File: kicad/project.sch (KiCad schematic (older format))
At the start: 21 parts, among them J1 SWD, U1 STM32L031F4Px

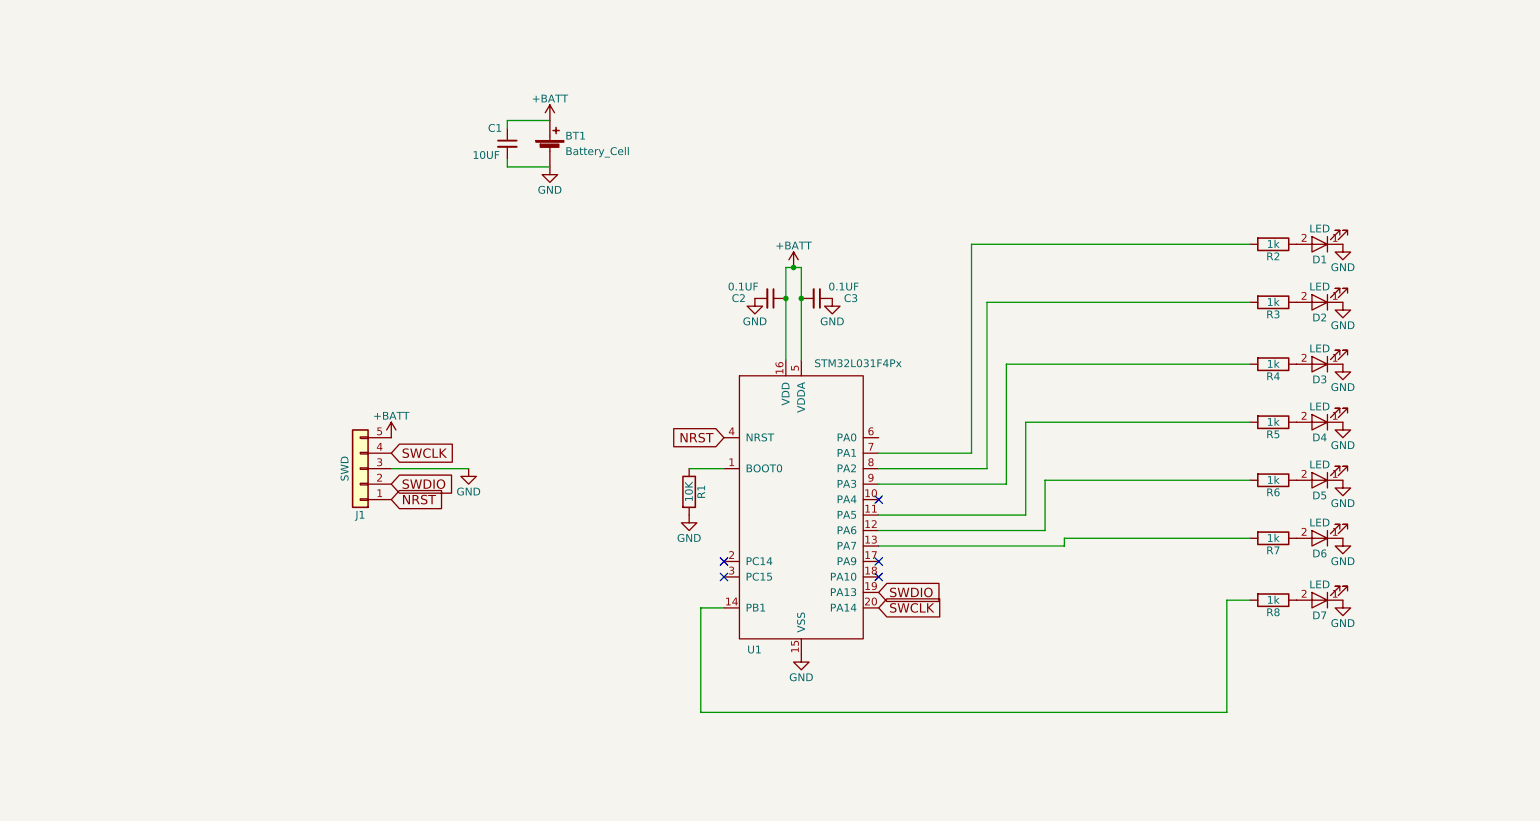
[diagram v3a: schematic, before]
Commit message: Power switch
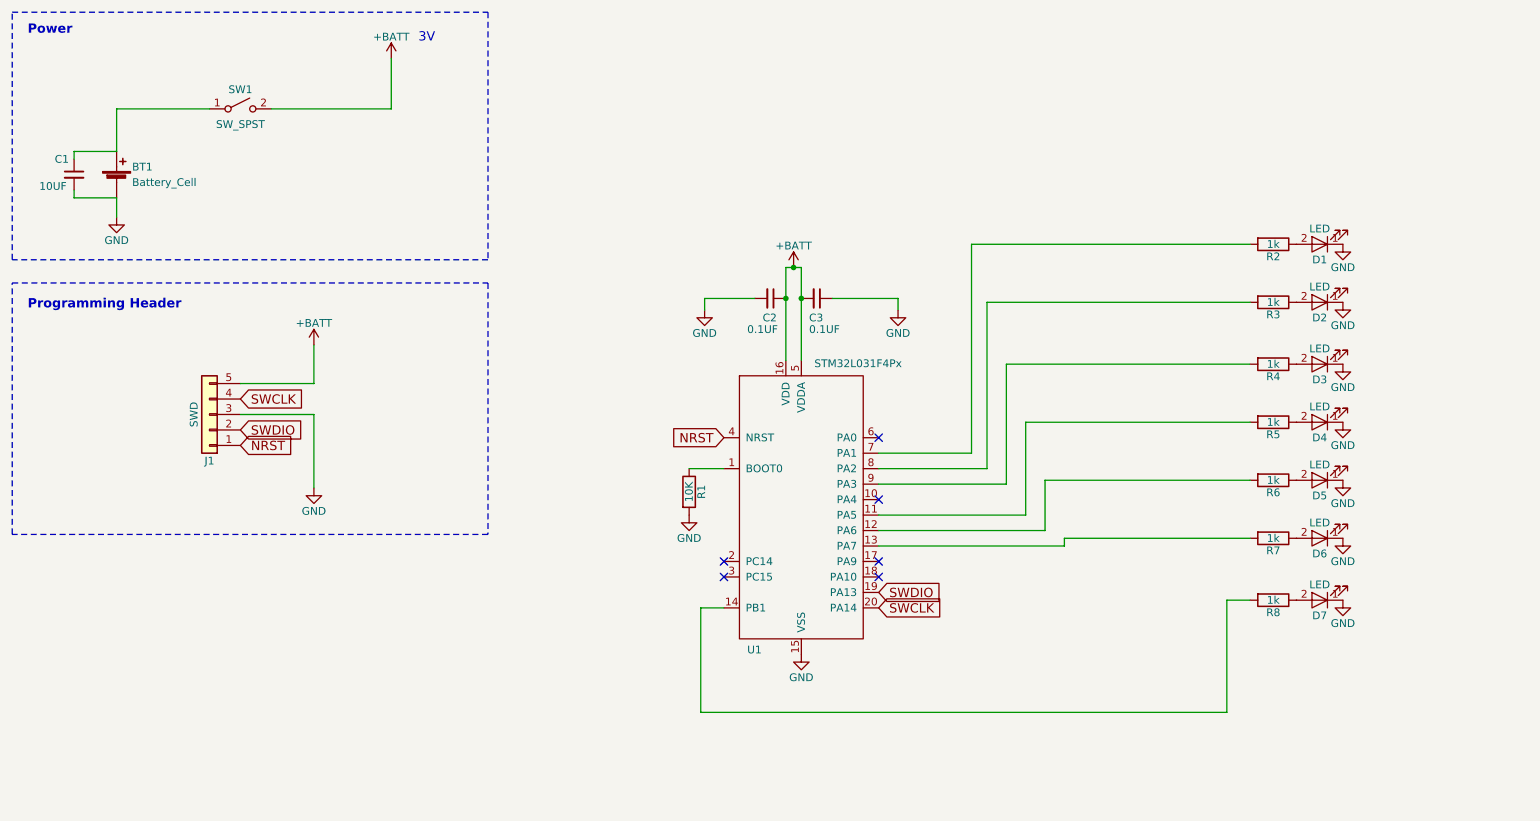
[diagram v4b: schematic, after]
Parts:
- added SW1: SW_SPST, Buttons_Switches_THT:SW_Tactile_Straight_KSA0Axx1LFTR, symbol SW_SPST
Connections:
- net +BATT: now also SW1.2 (B); no longer BT1.1 (+), C1.1
- new net: BT1.1 (+), C1.1, SW1.1 (A)
- no-connect marks 5 -> 6
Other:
- note added: "3V"
- note added: "Power"
- note added: "Programming Header"
- moved on the sheet: BT1, C1, J1

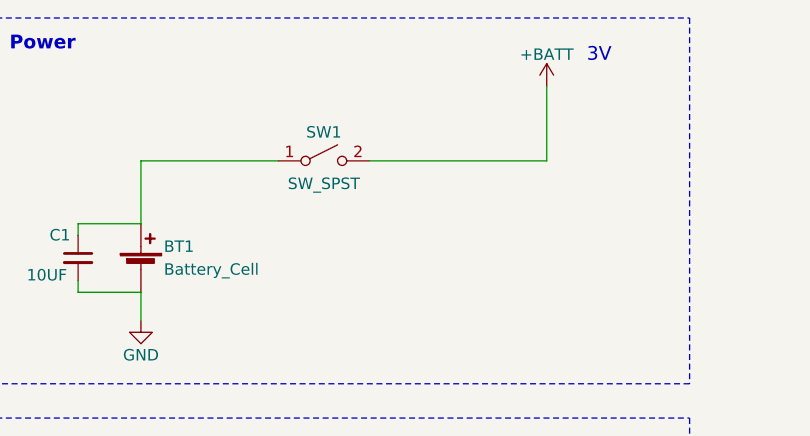
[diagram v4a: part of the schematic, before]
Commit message: 3 pin push switch
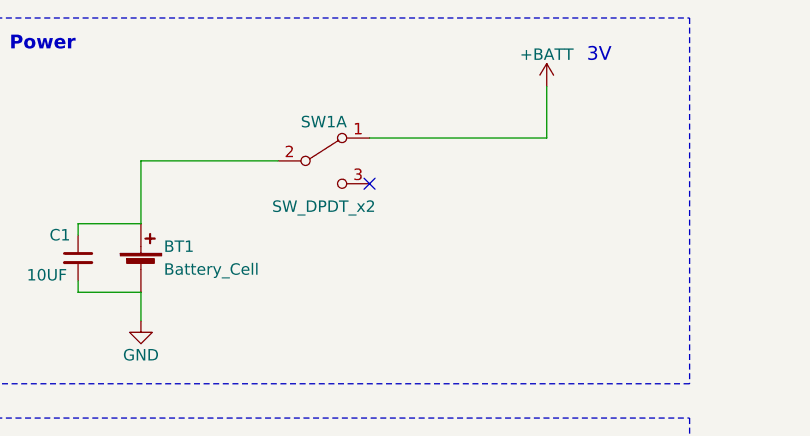
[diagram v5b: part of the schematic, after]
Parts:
- removed SW1: SW_SPST, Buttons_Switches_THT:SW_Tactile_Straight_KSA0Axx1LFTR, symbol SW_SPST
- added SW1: SW_DPDT_x2, Buttons_Switches_THT:SW_Micro_SPST, symbol SW_DPDT_x2
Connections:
- net +BATT: now also SW1.1 (A)
- net at BT1.1 (+), C1.1: now also SW1.2 (B)
- no-connect marks 6 -> 7
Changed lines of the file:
@@
 Wire Wire Line
 	1250 1300 1250 1575
-Wire Wire Line
-	2250 1300 3025 1300
 Text Notes 3200 875  0    60   ~ 0
 3V
@@
 	1250 1300 1850 1300
 Wire Wire Line
-	3025 1300 3025 975
-Wire Wire Line
 	1250 2000 1250 1875
-$Comp
-L SW_SPST SW1
-U 1 1 5AA2904E
-P 2050 1300
-F 0 "SW1" H 2050 1425 50  0000 C CNN
-F 1 "SW_SPST" H 2050 1200 50  0000 C CNN
-F 2 "Buttons_Switches_THT:SW_Tactile_Straight_KSA0Axx1LFTR" H 2050 1300 50  0001 C CNN
-F 3 "" H 2050 1300 50  0001 C CNN
-	1    2050 1300
-	1    0    0    -1
-$EndComp
 Wire Notes Line
 	575  2425 3650 2425
@@
 	6300 2525 6300 2600
 NoConn ~ 6175 3425
+$Comp
+L SW_DPDT_x2 SW1
+U 1 1 5AA401EC
+P 2050 1300
+F 0 "SW1" H 2050 1470 50  0000 C CNN
+F 1 "SW_DPDT_x2" H 2050 1100 50  0000 C CNN
+F 2 "Buttons_Switches_THT:SW_Micro_SPST" H 2050 1300 50  0001 C CNN
+F 3 "" H 2050 1300 50  0001 C CNN
+	1    2050 1300
+	1    0    0    -1
+$EndComp
+Wire Wire Line
+	2250 1200 3025 1200
+Wire Wire Line
+	3025 1200 3025 975
+NoConn ~ 2250 1400
 $EndSCHEMATC

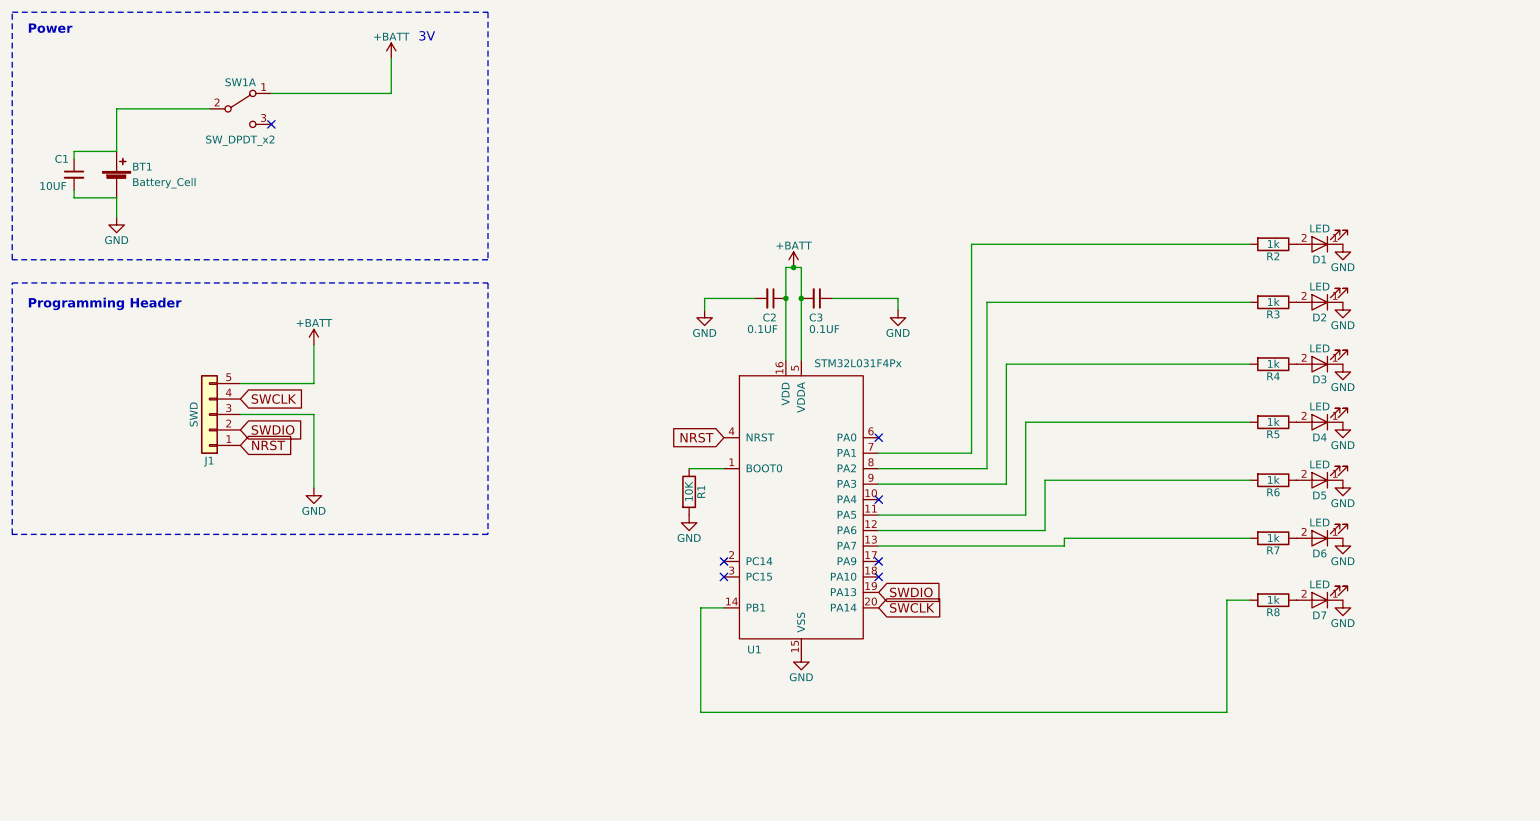
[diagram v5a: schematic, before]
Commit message: Optional LED footprints
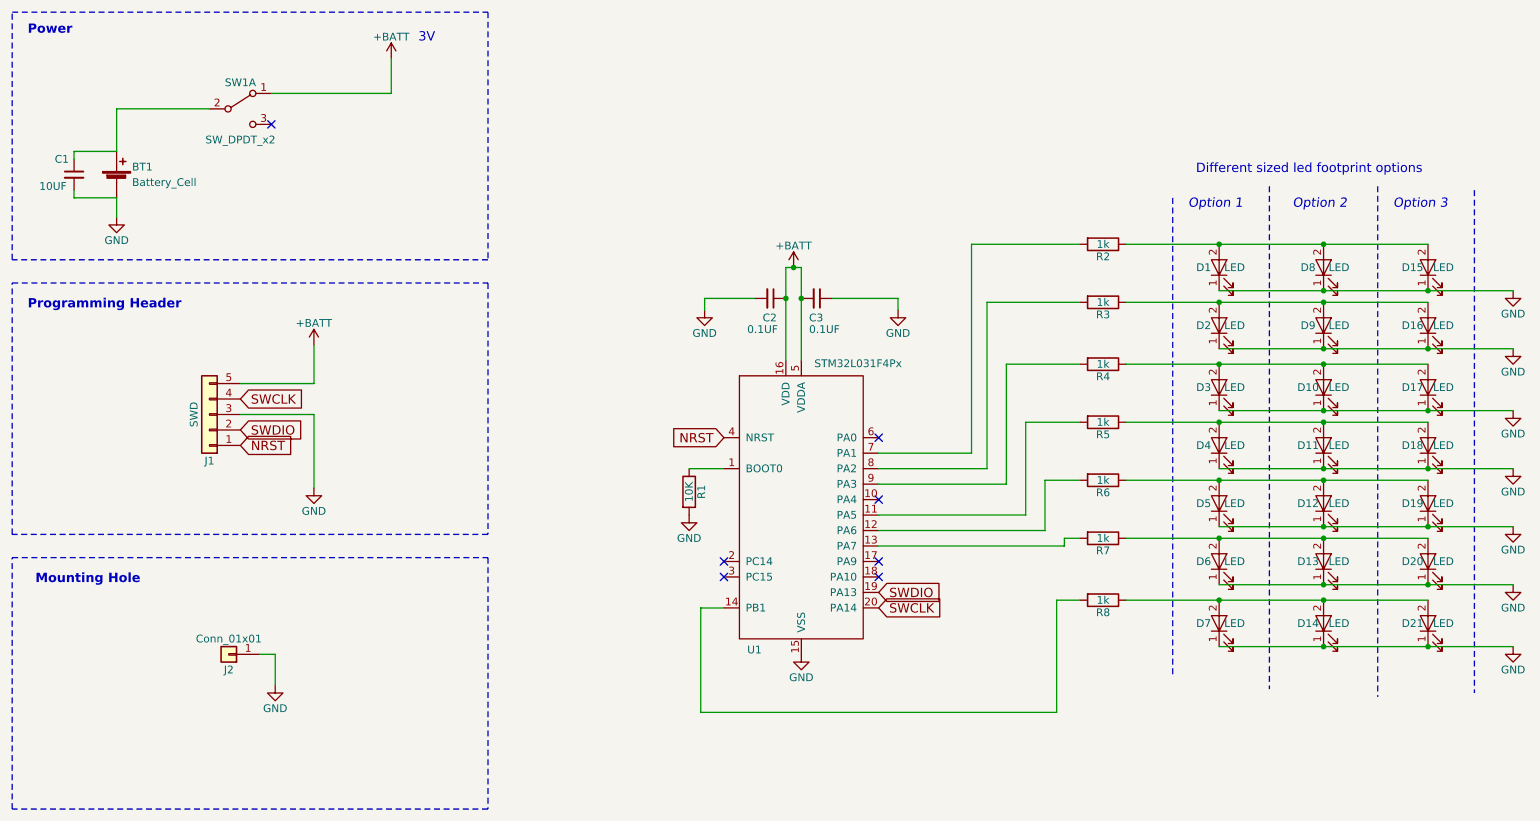
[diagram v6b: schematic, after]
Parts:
- added D10, D11, D12, D13, D14, D8, D9: LED, LEDs:LED_D5.0mm, symbol LED
- added D15, D16, D17, D18, D19, D20, D21: LED, LEDs:LED_1206, symbol LED
- added J2: Conn_01x01, Mounting_Holes:MountingHole_2.5mm, symbol Conn_01x01
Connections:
- net GND: now also D10.1 (K), D11.1 (K), D12.1 (K), D13.1 (K), D14.1 (K), D15.1 (K), D16.1 (K), D17.1 (K), D18.1 (K), D19.1 (K), D20.1 (K), D21.1 (K), D8.1 (K), D9.1 (K), J2.1 (Pin_1)
- net at D1.2 (A), R2.1: now also D15.2 (A), D8.2 (A)
- net at D2.2 (A), R3.1: now also D16.2 (A), D9.2 (A)
- net at D3.2 (A), R4.1: now also D10.2 (A), D17.2 (A)
- net at D4.2 (A), R5.1: now also D11.2 (A), D18.2 (A)
- net at D5.2 (A), R6.1: now also D12.2 (A), D19.2 (A)
- net at D6.2 (A), R7.1: now also D13.2 (A), D20.2 (A)
- net at D7.2 (A), R8.1: now also D14.2 (A), D21.2 (A)
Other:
- note added: "Different sized led footprint options"
- note added: "Mounting Hole"
- note added: "Option 1"
- note added: "Option 2"
- note added: "Option 3"
- moved on the sheet: D1, D2, D3, D4, D5, D6, D7, R2, R3, R4, R5, R6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

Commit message: LEDs layout
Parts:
- removed D14: LED, LEDs:LED_D5.0mm, symbol LED
- removed D21: LED, LEDs:LED_1206, symbol LED
- removed D7: LED, LEDs:LED_0805, symbol LED
- removed R8: 1k, Resistors_SMD:R_0603_HandSoldering, symbol R
- J1: value SWD -> Conn_01x05
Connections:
- net +BATT: now also J1.1 (Pin_1); no longer J1.5 (Pin_5)
- net NRST: now also J1.5 (Pin_5); no longer J1.1 (Pin_1)
- net SWCLK: now also J1.2 (Pin_2); no longer J1.4 (Pin_4)
- net SWDIO: now also J1.4 (Pin_4); no longer J1.2 (Pin_2)
- no-connect marks 7 -> 8
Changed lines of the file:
@@
-$EndComp
-$Comp
-L Conn_01x05 J1
-U 1 1 5A9FF0BA
-P 1850 3275
-F 0 "J1" H 1850 3575 50  0000 C CNN
-F 1 "SWD" V 1950 3275 50  0000 C CNN
-F 2 "Pin_Headers:Pin_Header_Straight_1x05_Pitch2.54mm" H 1850 3275 50  0001 C CNN
-F 3 "" H 1850 3275 50  0001 C CNN
-	1    1850 3275
-	-1   0    0    1
 $EndComp
 $Comp
@@
 F 3 "" H 7625 4075 50  0001 C CNN
 	1    7625 4075
-	0    1    1    0
-$EndComp
-$Comp
-L LED D7
-U 1 1 5A9FFC1D
-P 8375 4625
-F 0 "D7" V 8375 4725 50  0000 C CNN
-F 1 "LED" V 8375 4525 50  0000 C CNN
-F 2 "LEDs:LED_0805" H 8375 4625 50  0001 C CNN
-F 3 "" H 8375 4625 50  0001 C CNN
-	1    8375 4625
-	0    -1   -1   0
-$EndComp
-$Comp
-L GND #PWR016
-U 1 1 5A9FFC23
-P 10275 4775
-F 0 "#PWR016" H 10275 4525 50  0001 C CNN
-F 1 "GND" H 10275 4625 50  0000 C CNN
-F 2 "" H 10275 4775 50  0001 C CNN
-F 3 "" H 10275 4775 50  0001 C CNN
-	1    10275 4775
-	1    0    0    -1
-$EndComp
-$Comp
-L R R8
-U 1 1 5A9FFC29
-P 7625 4475
-F 0 "R8" V 7705 4475 50  0000 C CNN
-F 1 "1k" V 7625 4475 50  0000 C CNN
-F 2 "Resistors_SMD:R_0603_HandSoldering" V 7555 4475 50  0001 C CNN
-F 3 "" H 7625 4475 50  0001 C CNN
-	1    7625 4475
 	0    1    1    0
 $EndComp
@@
 NoConn ~ 2250 1400
 $Comp
-L GND #PWR017
+L GND #PWR016
 U 1 1 5AAE815A
 P 2275 5025
-F 0 "#PWR017" H 2275 4775 50  0001 C CNN
+F 0 "#PWR016" H 2275 4775 50  0001 C CNN
 F 1 "GND" H 2275 4875 50  0000 C CNN
 F 2 "" H 2275 5025 50  0001 C CNN
@@
 	7375 4075 7475 4075
 Wire Wire Line
-	5175 4525 5025 4525
-Wire Wire Line
-	5025 4525 5025 5200
-Wire Wire Line
-	5025 5200 7325 5200
-Wire Wire Line
-	7325 5200 7325 4475
-Wire Wire Line
-	7325 4475 7475 4475
-Wire Wire Line
 	1250 1300 1250 1575
 Wire Notes Line
@@
 $EndComp
 $Comp
-L LED D14
-U 1 1 5AAEB266
-P 9050 4625
-F 0 "D14" V 9050 4725 50  0000 C CNN
-F 1 "LED" V 9050 4525 50  0000 C CNN
-F 2 "LEDs:LED_D5.0mm" H 9050 4625 50  0001 C CNN
-F 3 "" H 9050 4625 50  0001 C CNN
-	1    9050 4625
-	0    -1   -1   0
-$EndComp
-$Comp
 L LED D15
 U 1 1 5AAEB486
@@
 	0    -1   -1   0
 $EndComp
-$Comp
-L LED D21
-U 1 1 5AAEB4AA
-P 9725 4625
-F 0 "D21" V 9725 4725 50  0000 C CNN
-F 1 "LED" V 9725 4525 50  0000 C CNN
-F 2 "LEDs:LED_1206" H 9725 4625 50  0001 C CNN
-F 3 "" H 9725 4625 50  0001 C CNN
-	1    9725 4625
-	0    -1   -1   0
-$EndComp
 Wire Wire Line
 	7775 2175 9725 2175
@@
 Connection ~ 9050 2475
 Connection ~ 9725 2475
-Wire Notes Line
-	9400 1800 9400 5100
-Wire Notes Line
-	8700 1800 8700 5050
-Wire Notes Line
-	10025 1825 10025 5075
-Wire Notes Line
-	8075 1875 8075 4975
 Text Notes 8175 1950 0    60   Italic 0
 Option 1
@@
 Connection ~ 9050 4375
 Connection ~ 9725 4375
-Wire Wire Line
-	7775 4475 9725 4475
-Connection ~ 8375 4475
-Connection ~ 9050 4475
-Wire Wire Line
-	8375 4775 10275 4775
-Connection ~ 9050 4775
-Connection ~ 9725 4775
+NoConn ~ 5175 4525
+$Comp
+L Conn_01x05 J1
+U 1 1 5AAE9626
+P 1850 3275
+F 0 "J1" H 1850 3575 50  0000 C CNN
+F 1 "Conn_01x05" H 1850 2975 50  0000 C CNN
+F 2 "Pin_Headers:Pin_Header_Straight_1x05_Pitch2.54mm" H 1850 3275 50  0001 C CNN
+F 3 "" H 1850 3275 50  0001 C CNN
+	1    1850 3275
+	-1   0    0    -1
+$EndComp
 $EndSCHEMATC

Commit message: Routing
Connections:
- net BATT_UNSWITCHED: now reaches BT1.1 (+), C1.1, SW1.2 (B)
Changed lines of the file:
@@
 	-1   0    0    -1
 $EndComp
+Text Label 1825 1300 2    60   ~ 0
+BATT_UNSWITCHED
 $EndSCHEMATC
